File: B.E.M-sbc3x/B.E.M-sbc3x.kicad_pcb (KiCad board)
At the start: 2 copper layers, 80 parts, among them CN1 Conn_02x13_Odd_Even, CN2 Conn_02x13_Odd_Even, CN3 Conn_02x13_Odd_Even, CN5 Conn_02x05_Odd_Even, CN6 Conn_02x05_Odd_Even, J1 Screw_Terminal_01x02, Q1 BD136, Q2 BC556, Q3 BC547, Q4 BC547, Q5 BC547, Q6 BC547, Q7 BC547, Q8 BC547, U1 TC55257PL-12, U10 74LS00, U11 74HC04, U12 CD4060BCN, U13 6822, U14 6822, U15 MM58274BN, U2 TC55257PL-12, U3 27256, U4 MC68A09, U5 6822, U6 TL7705ACPSR, U7 INS2651, U8 DM74S571, U9 74LS42, X1 32.768, X2 5.0688, X3 4.000

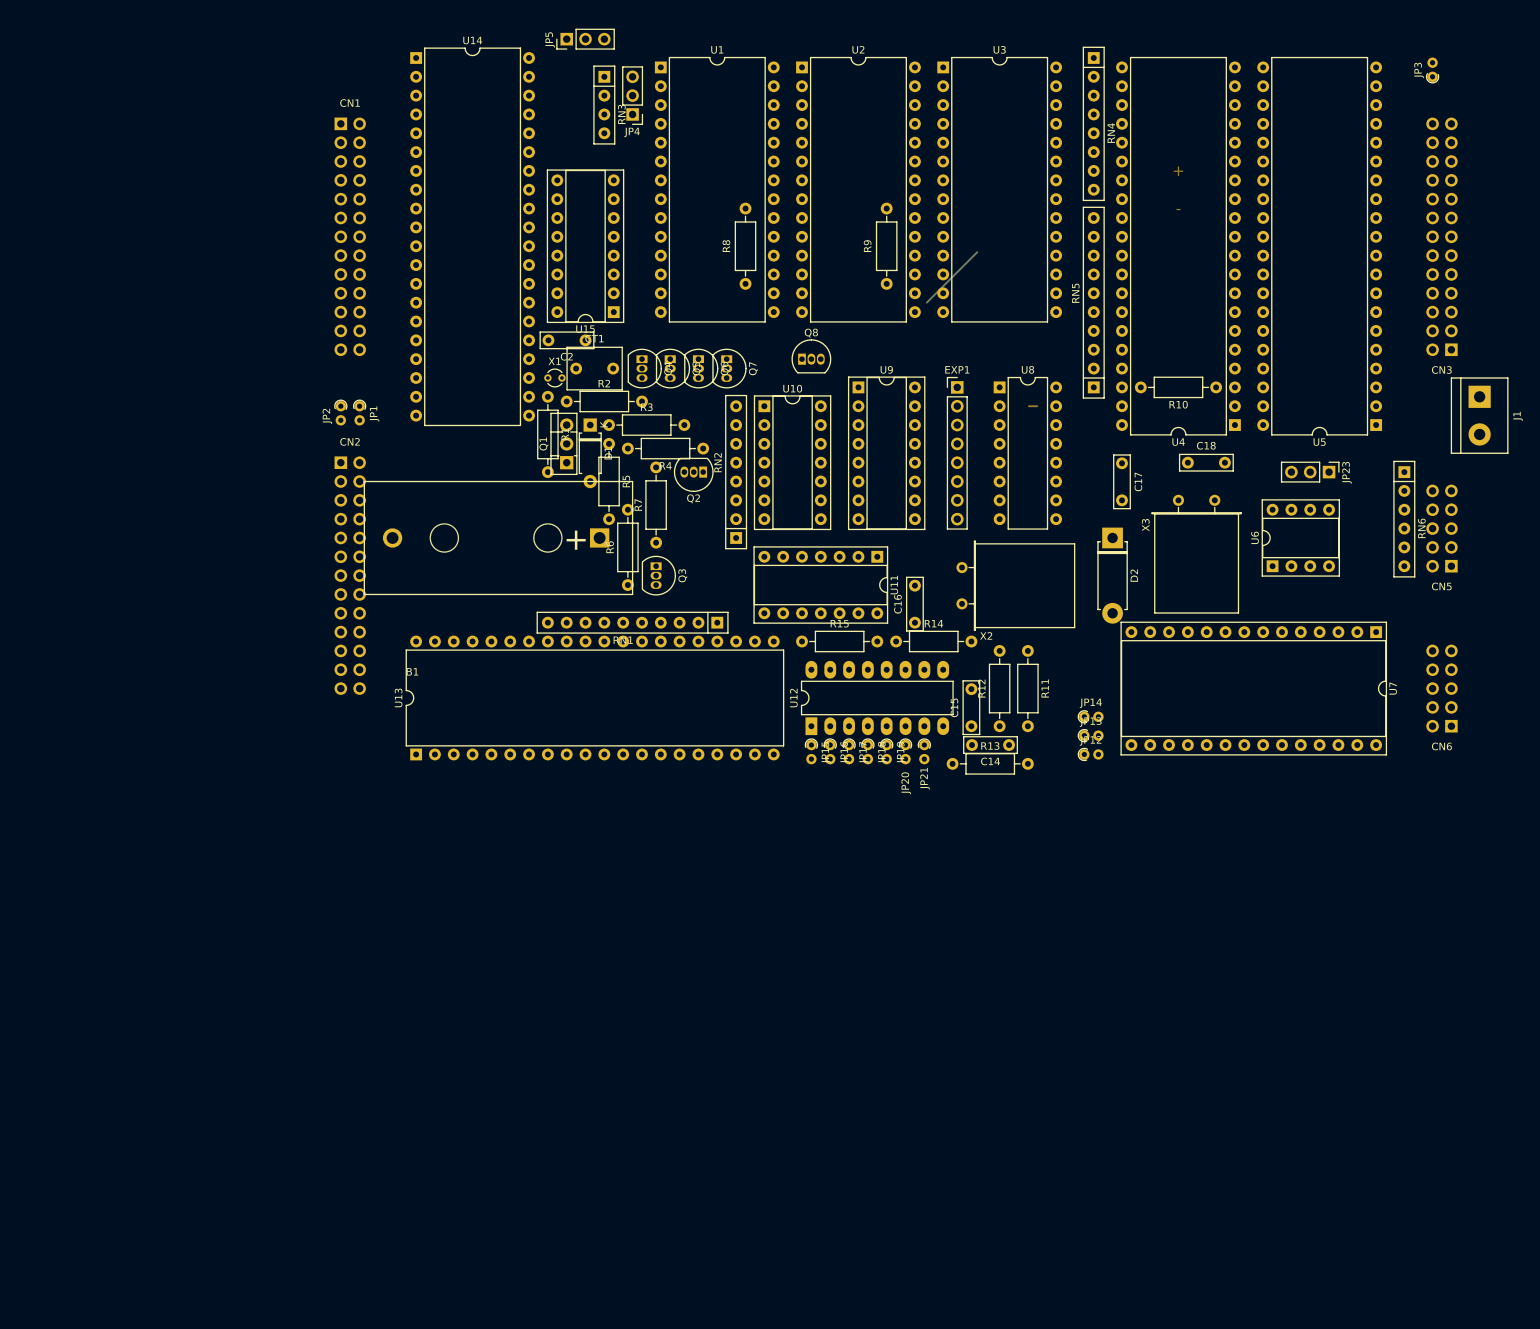
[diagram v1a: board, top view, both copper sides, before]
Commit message: All connectors are mapped, daughter DATAC-1A mapped, components all placed on PCB, HD46508PA added to library
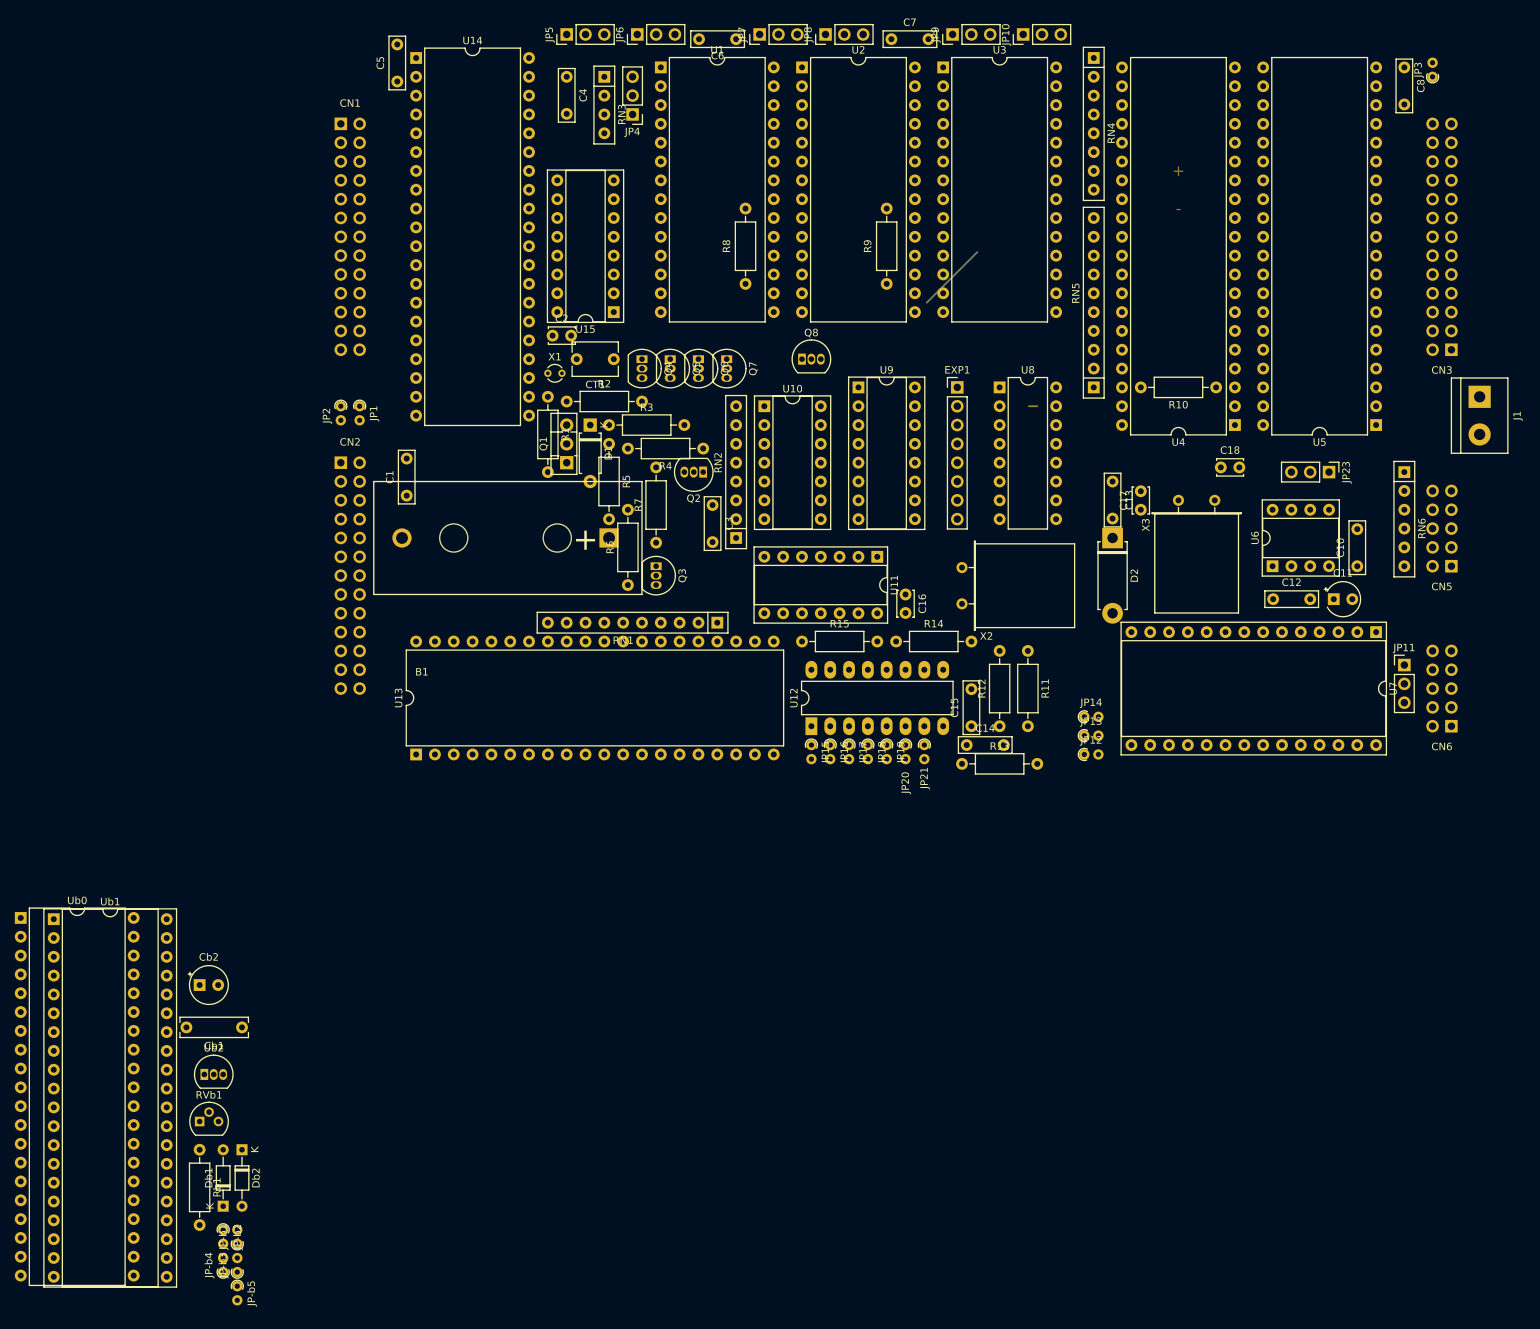
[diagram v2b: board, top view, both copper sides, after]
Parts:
- added C1: 100nF, Capacitor_THT:C_Rect_L7.0mm_W2.0mm_P5.00mm, F.Cu at (76.2, 84.5)
- added C10: 100nF, Capacitor_THT:C_Rect_L7.0mm_W2.0mm_P5.00mm, F.Cu at (204.5, 94.0)
- added C11: 10uF, Capacitor_THT:CP_Radial_Tantal_D4.5mm_P2.50mm, F.Cu at (201.3, 98.4)
- added C12: 100nF, Capacitor_THT:C_Rect_L7.0mm_W2.0mm_P5.00mm, F.Cu at (193.1, 98.4)
- added C13: 100nF, Capacitor_THT:C_Rect_L7.0mm_W2.0mm_P5.00mm, F.Cu at (171.4, 82.5)
- added C3: 100nF, Capacitor_THT:C_Rect_L7.0mm_W2.0mm_P5.00mm, F.Cu at (117.5, 85.7)
- added C4: 100nF, Capacitor_THT:C_Rect_L7.0mm_W2.0mm_P5.00mm, F.Cu at (97.8, 27.9)
- added C5: 100nF, Capacitor_THT:C_Rect_L7.0mm_W2.0mm_P5.00mm, F.Cu at (74.9, 28.6)
- added C6: 100nF, Capacitor_THT:C_Rect_L7.0mm_W2.0mm_P5.00mm, F.Cu at (120.7, 22.9)
- added C7: 100nF, Capacitor_THT:C_Rect_L7.0mm_W2.0mm_P5.00mm, F.Cu at (141.6, 22.9)
- added C8: 100nF, Capacitor_THT:C_Rect_L7.0mm_W2.0mm_P5.00mm, F.Cu at (210.8, 26.7)
- added Cb1: 100nF, Capacitor_THT:C_Rect_L9.0mm_W2.5mm_P7.50mm_MKT, F.Cu at (54.0, 156.2)
- added Cb2: 100pF, Capacitor_THT:CP_Radial_Tantal_D5.0mm_P2.50mm, F.Cu at (48.3, 150.5)
- added Db1: 1n4148, Diode_THT:D_DO-34_SOD68_P7.62mm_Horizontal, F.Cu at (51.4, 180.3)
- added Db2: 1n4148, Diode_THT:D_DO-34_SOD68_P7.62mm_Horizontal, F.Cu at (54.0, 172.7)
- added JP-b1: Device_Jumper_NO_Small, Resistor_THT:R_Axial_DIN0204_L3.6mm_D1.6mm_P1.90mm_Vertical, F.Cu at (53.3, 185.4)
- added JP-b2: Device_Jumper_NO_Small, Resistor_THT:R_Axial_DIN0204_L3.6mm_D1.6mm_P1.90mm_Vertical, F.Cu at (51.4, 183.5)
- added JP-b3: Device_Jumper_NO_Small, Resistor_THT:R_Axial_DIN0204_L3.6mm_D1.6mm_P1.90mm_Vertical, F.Cu at (53.3, 189.2)
- added JP-b4: Device_Jumper_NO_Small, Resistor_THT:R_Axial_DIN0204_L3.6mm_D1.6mm_P1.90mm_Vertical, F.Cu at (51.4, 189.2)
- added JP-b5: Device_Jumper_NO_Small, Resistor_THT:R_Axial_DIN0204_L3.6mm_D1.6mm_P1.90mm_Vertical, F.Cu at (53.3, 191.1)
- added JP10: Jumper_3_Open, Connector_PinHeader_2.54mm:PinHeader_1x03_P2.54mm_Vertical, F.Cu at (159.4, 22.2)
- added JP11: Jumper_3_Open, Connector_PinHeader_2.54mm:PinHeader_1x03_P2.54mm_Vertical, F.Cu at (210.8, 107.3)
- added JP6: Jumper_3_Open, Connector_PinHeader_2.54mm:PinHeader_1x03_P2.54mm_Vertical, F.Cu at (107.3, 22.2)
- added JP7: Jumper_3_Open, Connector_PinHeader_2.54mm:PinHeader_1x03_P2.54mm_Vertical, F.Cu at (123.8, 22.2)
- added JP8: Jumper_3_Open, Connector_PinHeader_2.54mm:PinHeader_1x03_P2.54mm_Vertical, F.Cu at (132.7, 22.2)
- added JP9: Jumper_3_Open, Connector_PinHeader_2.54mm:PinHeader_1x03_P2.54mm_Vertical, F.Cu at (149.9, 22.2)
- added RVb1: R_POT, Package_TO_SOT_THT:TO-92, F.Cu at (48.3, 168.9)
- added Rb1: 2.2K, Resistor_THT:R_Axial_DIN0207_L6.3mm_D2.5mm_P10.16mm_Horizontal, F.Cu at (48.3, 172.7)
- added Ub0: 6822, Package_DIP:DIP-40_W15.24mm, F.Cu at (24.1, 141.4)
- added Ub1: HD46508PA, Package_DIP:DIP-40_W15.24mm_Socket, F.Cu at (28.6, 141.6)
- added Ub2: LM336, Package_TO_SOT_THT:TO-92_Inline, F.Cu at (48.9, 162.6)
- C14: value 100n -> 100nF
- C15: value 10n -> 100nF
- C16: footprint Capacitor_THT:C_Rect_L7.0mm_W2.0mm_P5.00mm -> Capacitor_THT:C_Disc_D3.4mm_W2.1mm_P2.50mm
- C17, C18: value 22p -> 22pF; footprint Capacitor_THT:C_Rect_L7.0mm_W2.0mm_P5.00mm -> Capacitor_THT:C_Disc_D3.4mm_W2.1mm_P2.50mm
- C2: value 22P -> 22pF; footprint Capacitor_THT:C_Rect_L7.0mm_W2.0mm_P5.00mm -> Capacitor_THT:C_Disc_D3.4mm_W2.1mm_P2.50mm
- CT1: value 30pF -> 6-30pF; footprint Capacitor_THT:C_Rect_L7.2mm_W5.5mm_P5.00mm_FKS2_FKP2_MKS2_MKP2 -> Capacitor_THT:C_Disc_D6.0mm_W4.4mm_P5.00mm
- moved C17 6.76 mm to (175.3, 86.4), turned to 90 degrees
- moved C14 5.72 mm to (151.8, 118.1), turned to 0 degrees
- moved CT1 5.24 mm to (104.1, 66.0), turned to 180 degrees
- moved C2 4.49 mm to (95.9, 62.9), turned to 0 degrees
- moved C18 4.49 mm to (186.1, 80.6)
- moved C16 4.02 mm to (143.5, 97.8), turned to 270 degrees
- moved B1 1.27 mm to (106.0, 90.2)
- moved R13 1.27 mm to (151.1, 120.7)
- moved X1 0.64 mm to (95.2, 67.9)
- moved JP5 0.63 mm to (97.8, 22.2)
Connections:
- C2 pad 1: (no net) -> Net-(C2-Pad1)
- CN1 pad 1: (no net) -> +5V
- CN1 pad 10: (no net) -> /C1-10
- CN1 pad 11: (no net) -> /C1-11
- CN1 pad 12: (no net) -> GND
- CN1 pad 13: (no net) -> GND
- CN1 pad 15: (no net) -> /C1-15
- CN1 pad 16: (no net) -> /C1-16
- CN1 pad 17: (no net) -> /C1-17
- CN1 pad 18: (no net) -> /C1-18
- CN1 pad 19: (no net) -> /C1-19
- CN1 pad 2: (no net) -> /C1-2
- CN1 pad 20: (no net) -> /C1-20
- CN1 pad 21: (no net) -> /C1-21
- CN1 pad 22: (no net) -> /C1-22
- CN1 pad 24: (no net) -> /C1-24
- CN1 pad 25: (no net) -> /C1-25
- CN1 pad 3: (no net) -> /C1-3
- CN1 pad 5: (no net) -> /C1-5
- CN1 pad 6: (no net) -> /C1-6
- CN1 pad 7: (no net) -> /C1-7
- CN1 pad 8: (no net) -> /C1-8
- CN1 pad 9: (no net) -> /C1-9
- CN2 pad 1: (no net) -> +5V
- CN2 pad 10: (no net) -> /C2-10
- CN2 pad 11: (no net) -> /C2-11
- CN2 pad 12: (no net) -> GND
- CN2 pad 13: (no net) -> GND
- CN2 pad 15: (no net) -> /C2-15
- CN2 pad 16: (no net) -> /C2-16
- CN2 pad 17: (no net) -> /C2-17
- CN2 pad 18: (no net) -> /C2-18
- CN2 pad 19: (no net) -> /C2-19
- CN2 pad 2: (no net) -> /C2-2
- CN2 pad 20: (no net) -> /C2-20
- CN2 pad 21: (no net) -> /C2-21
- CN2 pad 22: (no net) -> /C2-22
- CN2 pad 24: (no net) -> /C2-24
- CN2 pad 25: (no net) -> /C2-25
- CN2 pad 3: (no net) -> /C2-3
- CN2 pad 5: (no net) -> /C2-5
- CN2 pad 6: (no net) -> /C2-6
- CN2 pad 7: (no net) -> /C2-7
- CN2 pad 8: (no net) -> /C2-8
- CN2 pad 9: (no net) -> /C2-9
- CN3 pad 1: (no net) -> +5V
- CN3 pad 10: (no net) -> /C3-10
- CN3 pad 11: (no net) -> /C3-11
- CN3 pad 12: (no net) -> GND
- CN3 pad 13: (no net) -> GND
- CN3 pad 15: (no net) -> /C3-15
- CN3 pad 16: (no net) -> /C3-16
- CN3 pad 17: (no net) -> /C3-17
- CN3 pad 18: (no net) -> /C3-18
- CN3 pad 19: (no net) -> /C3-19
- CN3 pad 2: (no net) -> /C3-2
- CN3 pad 20: (no net) -> /C3-20
- CN3 pad 21: (no net) -> /C3-21
- CN3 pad 22: (no net) -> /C3-22
- CN3 pad 24: (no net) -> /C3-24
- CN3 pad 25: (no net) -> /C3-25
- CN3 pad 5: (no net) -> /C3-5
- CN3 pad 6: (no net) -> /C3-6
- CN3 pad 7: (no net) -> /C3-7
- CN3 pad 8: (no net) -> /C3-8
- CN3 pad 9: (no net) -> /C3-9
- CT1 pad 1: (no net) -> Net-(C2-Pad1)
- JP19 pad 1: Net-(JP19-Pad1) -> /C2-3
- JP20 pad 1: Net-(JP20-Pad1) -> /C2-25
- U1 pad 1: /A14 -> Net-(JP6-Pad2)
- U1 pad 28: +5V -> Net-(JP6-Pad2)
- U13 pad 10: (no net) -> /C2-15
- U13 pad 11: (no net) -> /C2-16
- U13 pad 12: (no net) -> /C2-17
- U13 pad 13: (no net) -> /C2-18
- U13 pad 14: (no net) -> /C2-19
- U13 pad 15: (no net) -> /C2-20
- U13 pad 16: (no net) -> /C2-21
- U13 pad 17: (no net) -> /C2-22
- U13 pad 18: (no net) -> /C2-24
- U13 pad 19: Net-(JP20-Pad1) -> /C2-25
- U13 pad 2: (no net) -> /C2-5
- U13 pad 3: (no net) -> /C2-6
- U13 pad 39: Net-(JP19-Pad1) -> /C2-3
- U13 pad 4: (no net) -> /C2-7
- U13 pad 40: (no net) -> /C2-2
- U13 pad 5: (no net) -> /C2-8
- U13 pad 6: (no net) -> /C2-9
- U13 pad 7: (no net) -> /C2-10
- U13 pad 8: (no net) -> /C2-11
- U13 pad 9: (no net) -> GND
- U14 pad 10: (no net) -> /C1-15
- U14 pad 11: (no net) -> /C1-16
- U14 pad 12: (no net) -> /C1-17
- U14 pad 13: (no net) -> /C1-18
- U14 pad 14: (no net) -> /C1-19
- U14 pad 15: (no net) -> /C1-20
- U14 pad 16: (no net) -> /C1-21
- U14 pad 17: (no net) -> /C1-22
- U14 pad 18: (no net) -> /C1-24
- U14 pad 19: (no net) -> /C1-25
- U14 pad 2: (no net) -> /C1-5
- U14 pad 3: (no net) -> /C1-6
- U14 pad 39: (no net) -> /C1-3
- U14 pad 4: (no net) -> /C1-7
- U14 pad 40: (no net) -> /C1-2
- U14 pad 5: (no net) -> /C1-8
- U14 pad 6: (no net) -> /C1-9
- U14 pad 7: (no net) -> /C1-10
- U14 pad 8: (no net) -> /C1-11
- U14 pad 9: (no net) -> GND
- U2 pad 1: /A14 -> Net-(JP7-Pad2)
- U2 pad 26: /A13 -> Net-(JP9-Pad2)
- U2 pad 28: +5V -> Net-(JP7-Pad3)
- U3 pad 1: (no net) -> +5V
- U3 pad 26: /A13 -> Net-(JP9-Pad3)
- U3 pad 27: /A14 -> Net-(JP10-Pad2)
- U5 pad 10: (no net) -> /C3-15
- U5 pad 11: (no net) -> /C3-16
- U5 pad 12: (no net) -> /C3-17
- U5 pad 13: (no net) -> /C3-18
- U5 pad 14: (no net) -> /C3-19
- U5 pad 15: (no net) -> /C3-20
- U5 pad 16: (no net) -> /C3-21
- U5 pad 17: (no net) -> /C3-22
- U5 pad 18: (no net) -> /C3-24
- U5 pad 19: (no net) -> /C3-25
- U5 pad 2: (no net) -> /C3-5
- U5 pad 3: (no net) -> /C3-6
- U5 pad 39: (no net) -> /C2-3
- U5 pad 4: (no net) -> /C3-7
- U5 pad 40: (no net) -> /C3-2
- U5 pad 5: (no net) -> /C3-8
- U5 pad 6: (no net) -> /C3-9
- U5 pad 7: (no net) -> /C3-10
- U5 pad 8: (no net) -> /C3-11
- U5 pad 9: (no net) -> GND
- U6 pad 1: (no net) -> Net-(C12-Pad1)
- U6 pad 3: (no net) -> Net-(C11-Pad1)
- U7 pad 10: /A0 -> /A1
- U7 pad 22: (no net) -> Net-(JP11-Pad1)
